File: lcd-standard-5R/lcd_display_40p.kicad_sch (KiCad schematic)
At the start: 53 parts, among them J10 CTP_10P, J5 CTP_6P, J6 LCD_40P, U7 XPT2046TS, U8 TPS61169

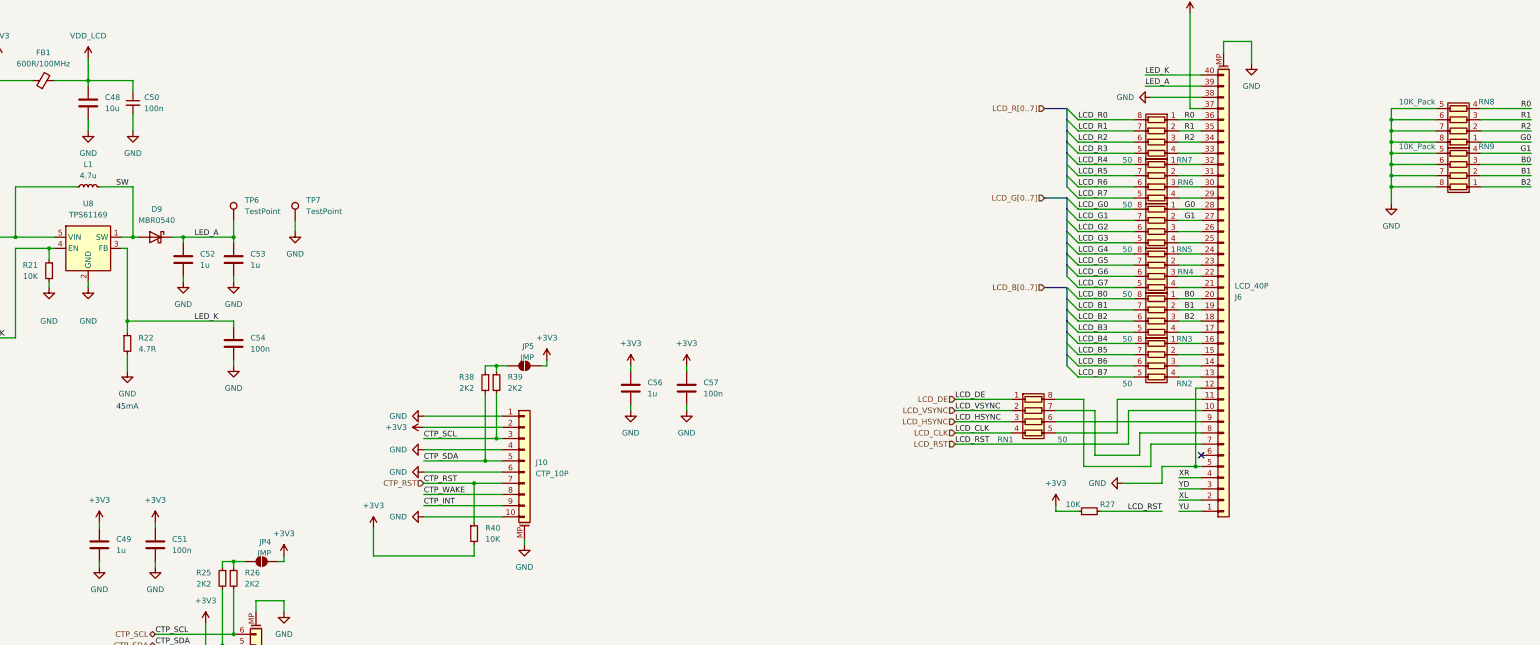
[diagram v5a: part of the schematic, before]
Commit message: Add QSPI Flash trace length matching to 5 inch LCD
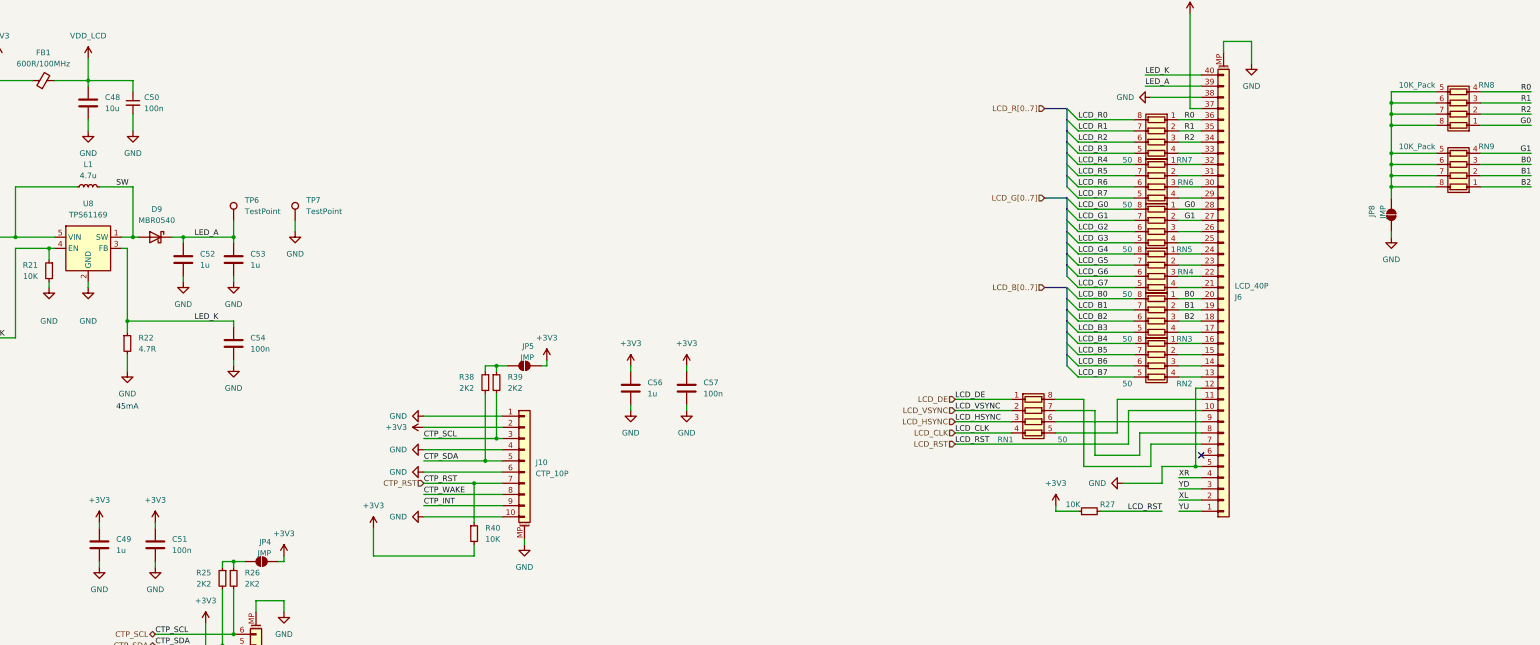
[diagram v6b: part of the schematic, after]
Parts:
- added JP8: JMP, Jumper:SolderJumper-2_P1.3mm_Open_RoundedPad1.0x1.5mm, symbol Jumper:SolderJumper_2_Open
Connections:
- net GND: now also JP8.1 (A); no longer RN8.5 (R4.2), RN8.6 (R3.2), RN8.7 (R2.2), RN8.8 (R1.2), RN9.5 (R4.2), RN9.6 (R3.2), RN9.7 (R2.2), RN9.8 (R1.2)
- new net: JP8.2 (B), RN8.5 (R4.2), RN8.6 (R3.2), RN8.7 (R2.2), RN8.8 (R1.2), RN9.5 (R4.2), RN9.6 (R3.2), RN9.7 (R2.2), RN9.8 (R1.2)
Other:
- moved on the sheet: RN8
